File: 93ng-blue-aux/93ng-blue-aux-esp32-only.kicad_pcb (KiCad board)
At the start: 2 copper layers, 24 parts, among them J1 12V INPUT, J2 ESP32 UART, J3 ESP32 JTAG, J7 I-BUS, SW1 SW_DIP_x01, U1 ESP32-WROOM-32D, U2 BA33DD0T, U3 MC33897

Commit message: More work on standalone ESP32 module
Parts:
- added C3: 1nF, Capacitor_SMD:C_0805_2012Metric_Pad1.15x1.40mm_HandSolder, F.Cu at (122.9, 79.0)
- added C6: 10uF, Capacitor_SMD:C_0805_2012Metric_Pad1.15x1.40mm_HandSolder, F.Cu at (104.9, 67.7)
- added C7: 10uF, Capacitor_SMD:C_0805_2012Metric_Pad1.15x1.40mm_HandSolder, F.Cu at (104.9, 70.7)
- added C8: 10uF, Capacitor_SMD:C_0805_2012Metric_Pad1.15x1.40mm_HandSolder, F.Cu at (109.6, 67.7)
- added D2: PWR_LED, LED_SMD:LED_0805_2012Metric_Pad1.15x1.40mm_HandSolder, F.Cu at (118.2, 79.0)
- added D4: 1N5819, Diode_THT:D_DO-41_SOD81_P10.16mm_Horizontal, F.Cu at (117.6, 67.1)
- added Q1: S8050, Package_TO_SOT_SMD:SOT-23_Handsoldering, F.Cu at (127.6, 78.0)
- added Q2: S8050, Package_TO_SOT_SMD:SOT-23_Handsoldering, F.Cu at (136.3, 68.3)
- added R11: 1K, Resistor_SMD:R_0805_2012Metric_Pad1.15x1.40mm_HandSolder, F.Cu at (139.2, 78.2)
- added R12: 470, Resistor_SMD:R_0805_2012Metric_Pad1.15x1.40mm_HandSolder, F.Cu at (144.0, 72.4)
- added R8: 12K, Resistor_SMD:R_0805_2012Metric_Pad1.15x1.40mm_HandSolder, F.Cu at (139.2, 75.2)
- added U4: FUSB302BMPX, Package_DFN_QFN:WQFN-14-1EP_2.5x2.5mm_P0.5mm_EP1.45x1.45mm, F.Cu at (138.1, 119.1)
- added U5: CP2102N-A01-GQFN28, Package_DFN_QFN:QFN-28-1EP_5x5mm_P0.5mm_EP3.35x3.35mm, F.Cu at (132.1, 120.4)
- C2: value 0.1uF -> 10uF
- J3: value ESP32 JTAG -> USB_C_Receptacle_USB2.0; footprint Connector_PinHeader_2.54mm:PinHeader_1x04_P2.54mm_Vertical -> Connector_USB:USB_C_Receptacle_Amphenol_12401610E4-2A
- R1: value 1k -> 12K
- R2: value 100 -> 2k
- R3, R4: value 100 -> 5k
- R5: value 100 -> 12K
- SW1: value SW_DIP_x01 -> PWR IN SELECT; footprint Button_Switch_SMD:SW_DIP_SPSTx01_Slide_Omron_A6S-110x_W8.9mm_P2.54mm -> Connector_PinHeader_2.54mm:PinHeader_1x03_P2.54mm_Vertical
- U2: value BA33DD0T -> NCP1117-3.3_SOT223; footprint Package_TO_SOT_THT:TO-220-3_Vertical -> Package_TO_SOT_SMD:SOT-223-3_TabPin2
- moved R4 68.4 mm to (143.2, 69.4)
- moved R1 64.8 mm to (143.2, 66.5)
- moved R5 58.7 mm to (134.5, 79.1)
- moved R3 54.6 mm to (134.5, 76.2)
- moved SW1 50.2 mm to (132.0, 67.3)
- moved J3 36.8 mm to (150.5, 114.0)
- moved R2 29.5 mm to (136.7, 72.3)
- moved U2 28.9 mm to (120.7, 73.4)
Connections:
- net Net-(J2-Pad1) renamed ESP32_RX
- net Net-(J2-Pad2) renamed ESP32_TX
- J1 pad 2: Net-(C1-Pad1) -> Net-(J1-Pad2)
- R1 pad 1: Net-(R1-Pad1) -> 3.3V
- R1 pad 2: 3.3V -> ESP32_EN
- R2 pad 1: Net-(J3-Pad4) -> Net-(D2-Pad2)
- R2 pad 2: Net-(R2-Pad2) -> 3.3V
- R3 pad 1: Net-(J3-Pad3) -> Net-(R3-Pad1)
- R3 pad 2: Net-(R3-Pad2) -> GND
- R4 pad 1: Net-(J3-Pad2) -> 3.3V
- R4 pad 2: Net-(R4-Pad2) -> ESP32_BOOT
- R5 pad 1: Net-(J3-Pad1) -> Net-(Q1-Pad2)
- R5 pad 2: Net-(R5-Pad2) -> DTR
- SW1 pad 1: ESP32_BOOTOPT -> Net-(J1-Pad2)
- SW1 pad 2: GND -> Net-(C1-Pad1)
- U1 pad 13: Net-(R5-Pad2) -> (no net)
- U1 pad 14: Net-(R4-Pad2) -> (no net)
- U1 pad 16: Net-(R3-Pad2) -> (no net)
- U1 pad 23: Net-(R2-Pad2) -> (no net)
- U1 pad 24: (no net) -> Net-(R3-Pad1)
- U1 pad 25: ESP32_BOOTOPT -> ESP32_BOOT
- U1 pad 3: Net-(R1-Pad1) -> ESP32_EN
- U2 pad 1: Net-(C1-Pad1) -> GND
- U2 pad 2: GND -> 3.3V
- U2 pad 3: 3.3V -> Net-(C1-Pad1)
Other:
- board outline added: 50 x 50 mm

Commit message: Playing with 50x50mm layout
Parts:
- removed J2: ESP32 UART, Connector_PinHeader_2.54mm:PinHeader_1x03_P2.54mm_Vertical
- moved U1 101.8 mm to (195.0, 88.0)
- moved D4 91.9 mm to (206.6, 90.0), turned to 90 degrees
- moved Q1 87.3 mm to (213.4, 93.8), turned to 180 degrees
- moved J7 85.3 mm to (198.1, 116.0)
- moved U4 82.4 mm to (210.2, 79.2), turned to 180 degrees
- moved U5 81.7 mm to (213.0, 108.8)
- moved J1 77.1 mm to (186.8, 116.0)
- moved Q2 76.8 mm to (207.8, 96.2), turned to 180 degrees
- moved U3 74.4 mm to (200.5, 104.0), turned to 270 degrees
- moved SW1 71.4 mm to (192.0, 106.0), turned to 270 degrees
- moved J3 69.4 mm to (214.2, 86.5), turned to 90 degrees
- moved U2 60.0 mm to (177.5, 92.5), turned to 90 degrees
- moved C1 48.5 mm to (177.5, 102.5), turned to 270 degrees

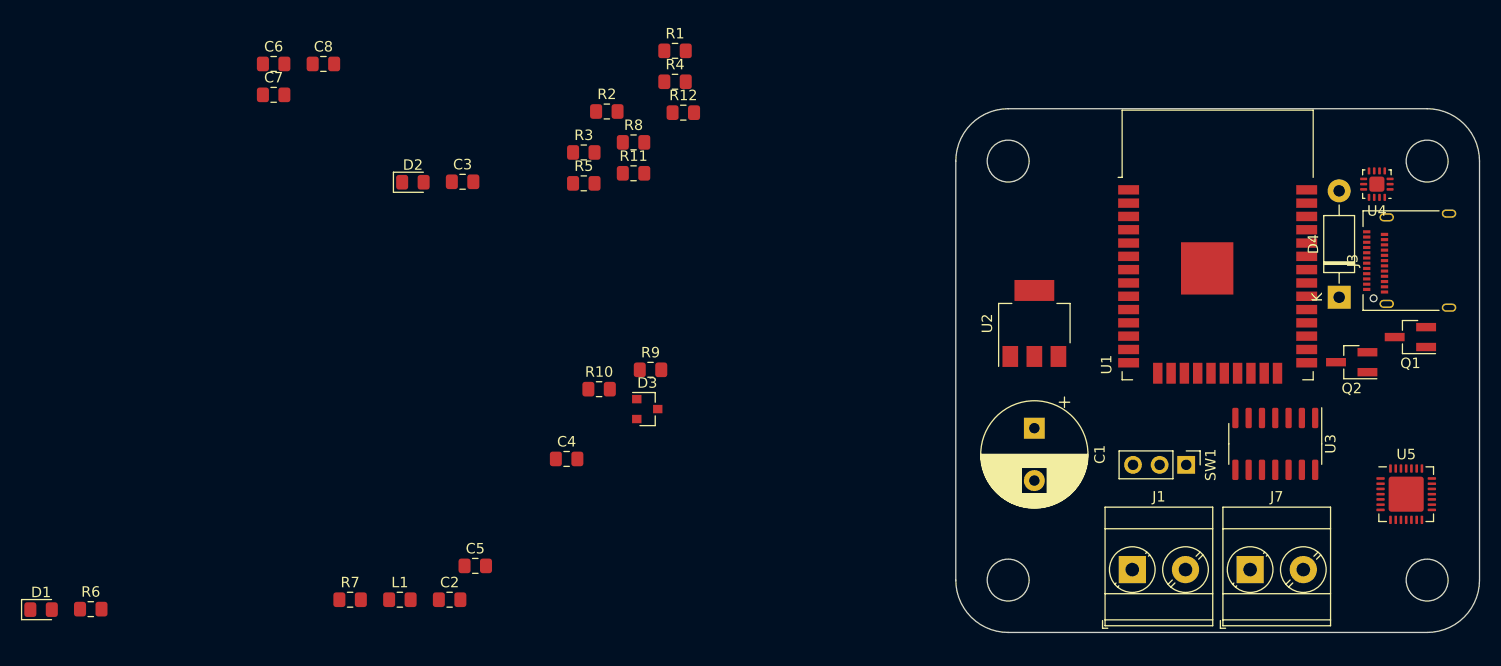
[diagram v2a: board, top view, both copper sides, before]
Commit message: Placed all the components roughly! Added ground plane!
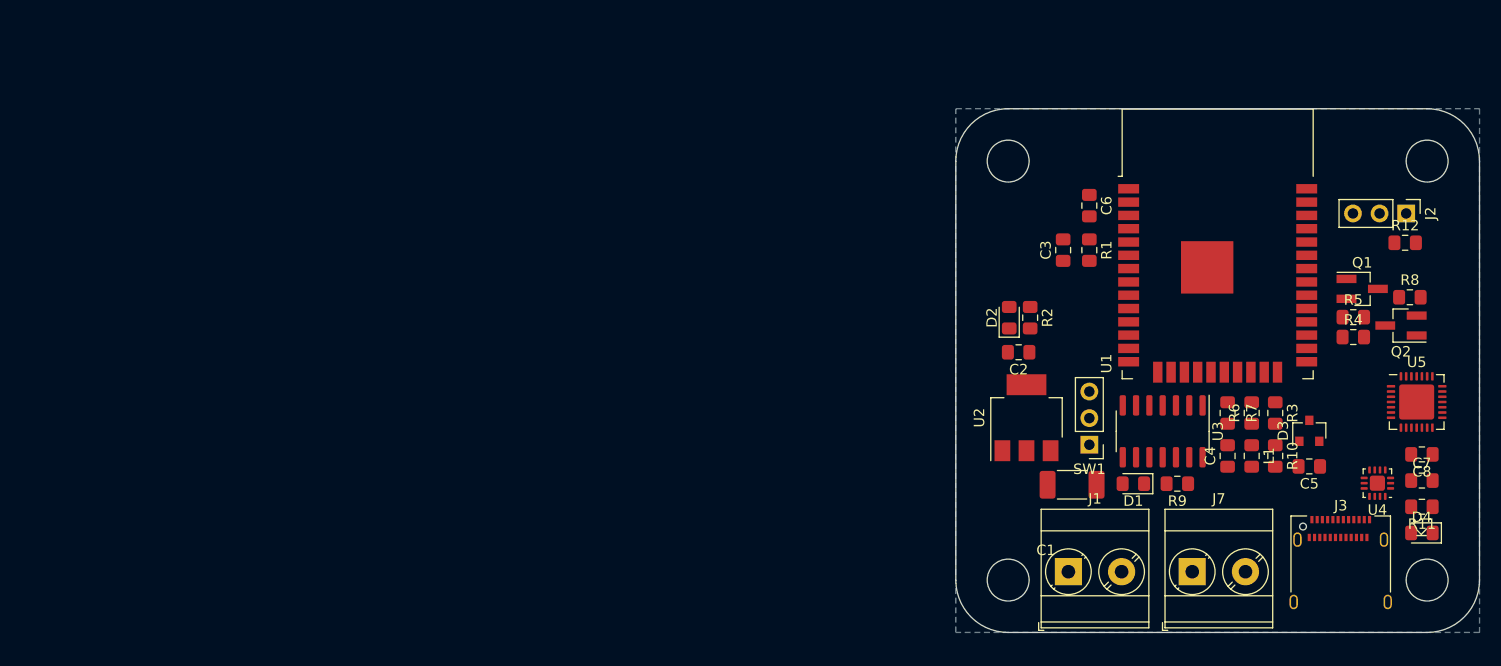
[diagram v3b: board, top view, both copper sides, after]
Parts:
- added J2: ESP32 UART, Connector_PinHeader_2.54mm:PinHeader_1x03_P2.54mm_Vertical, F.Cu at (213.0, 82.0)
- C1: footprint Capacitor_THT:CP_Radial_D10.0mm_P5.00mm -> Capacitor_SMD:C_2010_5025Metric_Pad1.52x2.65mm_HandSolder
- D4: footprint Diode_THT:D_DO-41_SOD81_P10.16mm_Horizontal -> Diode_SMD:D_0805_2012Metric_Pad1.15x1.40mm_HandSolder
- moved C7 115.6 mm to (214.5, 107.5)
- moved R6 112.4 mm to (198.2, 101.0), turned to 90 degrees
- moved C8 111.3 mm to (214.5, 105.0), turned to 180 degrees
- moved D1 105.0 mm to (186.9, 107.8), turned to 180 degrees
- moved R7 85.7 mm to (195.9, 101.0), turned to 270 degrees
- moved L1 82.5 mm to (198.2, 105.2), turned to 270 degrees
- moved R11 81.7 mm to (214.5, 110.0), turned to 180 degrees
- moved C5 80.2 mm to (203.8, 106.2), turned to 180 degrees
- moved C6 79.0 mm to (182.8, 81.2), turned to 270 degrees
- moved R8 75.6 mm to (213.3, 90.0)
- moved R5 74.6 mm to (207.9, 91.9)
- moved R3 70.5 mm to (200.5, 101.0), turned to 270 degrees
- moved R12 70.0 mm to (212.9, 84.8)
- moved R4 69.2 mm to (207.9, 93.8)
- moved R10 64.9 mm to (200.5, 105.2), turned to 270 degrees
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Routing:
- added copper zone on B.Cu, net GND

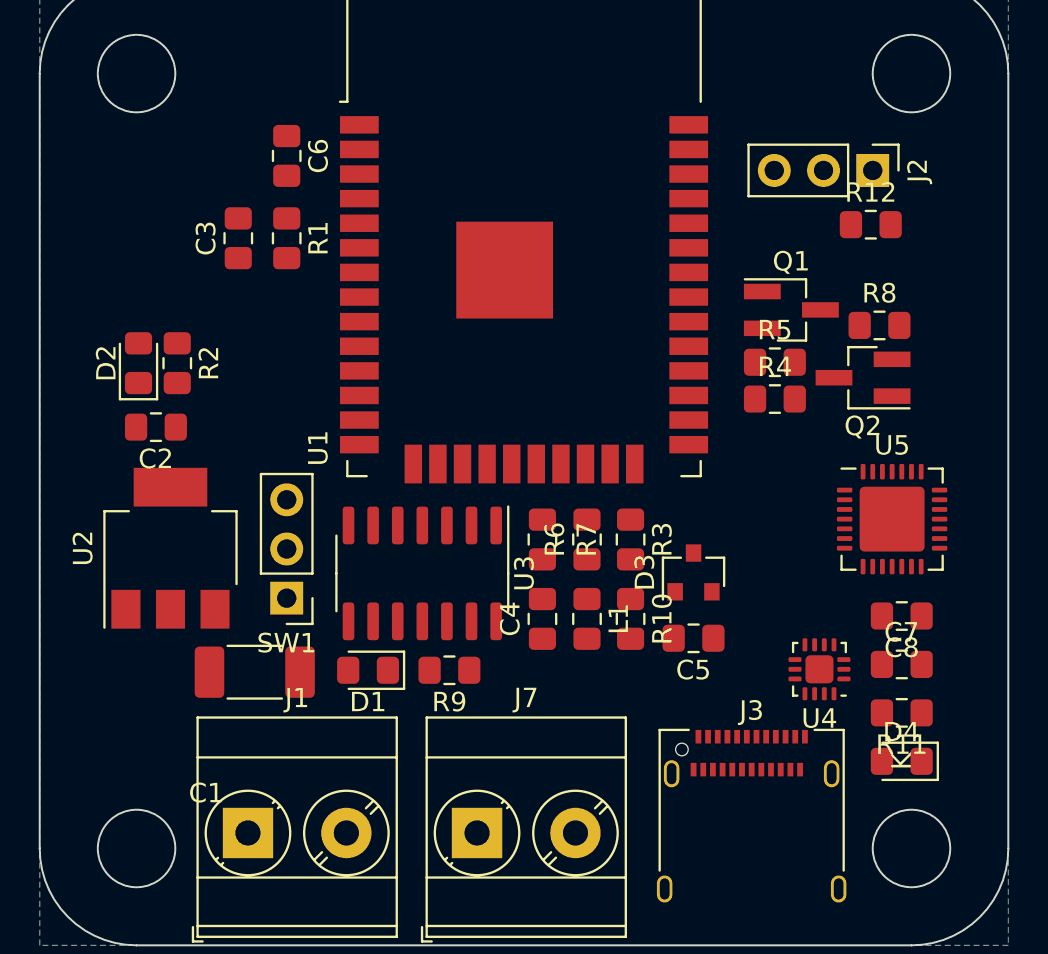
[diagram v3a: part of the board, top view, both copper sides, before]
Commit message: Did routing. Decided it looks horrible. Need to investigate better USB-C solution, remove the PD chip.
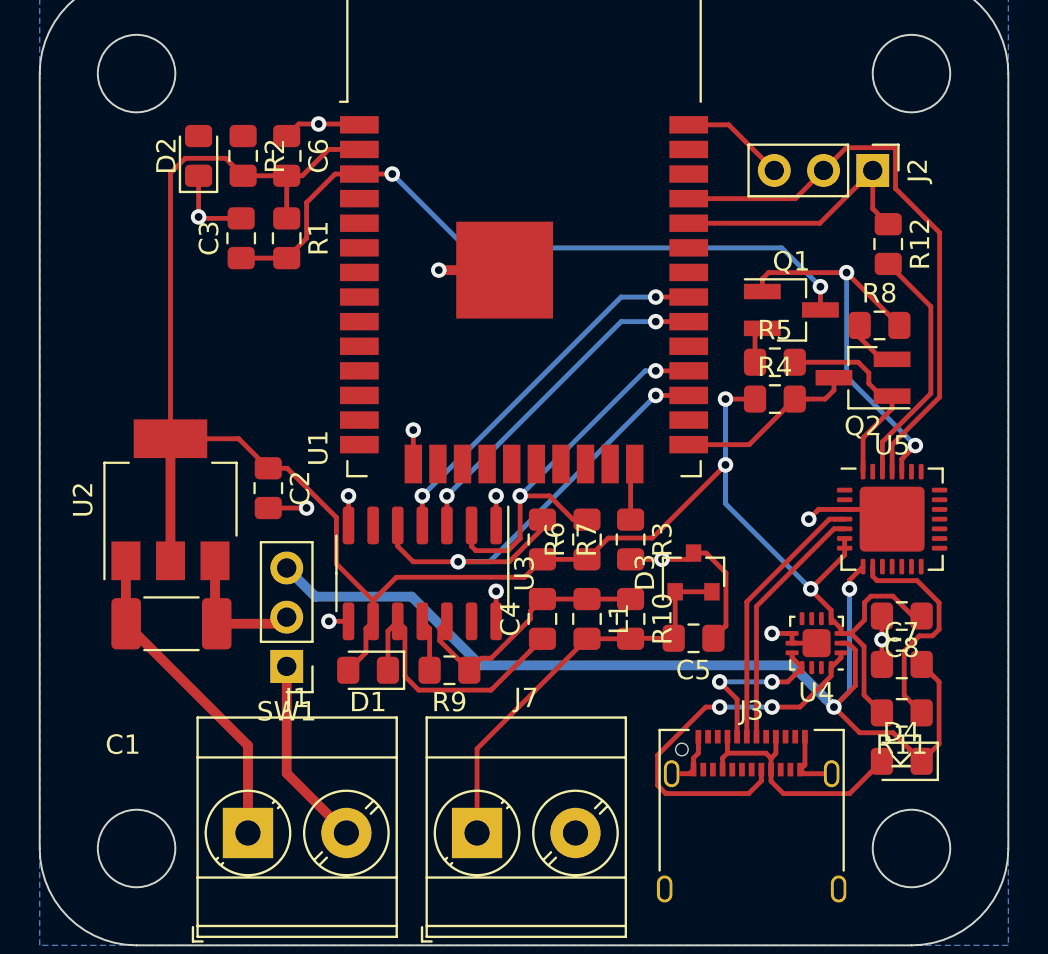
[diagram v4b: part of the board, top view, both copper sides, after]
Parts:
- moved R2 11.2 mm to (180.5, 81.2)
- moved D2 11.1 mm to (178.2, 81.2)
- moved C2 6.60 mm to (181.8, 98.4), turned to 270 degrees
- moved C1 4.97 mm to (176.8, 105.4)
- moved SW1 3.52 mm to (182.8, 107.6)
- moved U2 2.50 mm to (176.8, 99.0)
- moved U4 1.36 mm to (210.1, 106.4)
- moved R12 1.35 mm to (213.8, 85.8), turned to 270 degrees
- moved C3 0.15 mm to (180.4, 85.5)
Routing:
- net 3.3V: track 0.00 -> 103.9 mm, vias 0 -> 3
- net GND: track 0.00 -> 68.9 mm, vias 0 -> 13
- net USB_VBUS: track 0.00 -> 54.8 mm, vias 0 -> 2
- net ESP32_EN: track 0.00 -> 36.4 mm, vias 0 -> 2
- net ESP32_TX: track 0.00 -> 30.4 mm
- net MC33_RX: track 0.00 -> 25.5 mm, vias 0 -> 2
- net MC33_TX: track 0.00 -> 21.5 mm, vias 0 -> 2
- net SW_CAN: track 0.00 -> 21.2 mm
- net RTS: track 0.00 -> 21.0 mm, vias 0 -> 2
- net USB_CC2: track 0.00 -> 20.0 mm, vias 0 -> 2
- net MC33_MODE1: track 0.00 -> 19.5 mm, vias 0 -> 2
- net MC33_MODE0: track 0.00 -> 17.7 mm, vias 0 -> 2
- net Net-(C4-Pad1): track 0.00 -> 14.2 mm
- net USB_D+: track 0.00 -> 13.8 mm
- net ESP32_RX: track 0.00 -> 13.7 mm
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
